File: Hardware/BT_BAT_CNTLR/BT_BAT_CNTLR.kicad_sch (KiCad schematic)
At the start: 0 parts

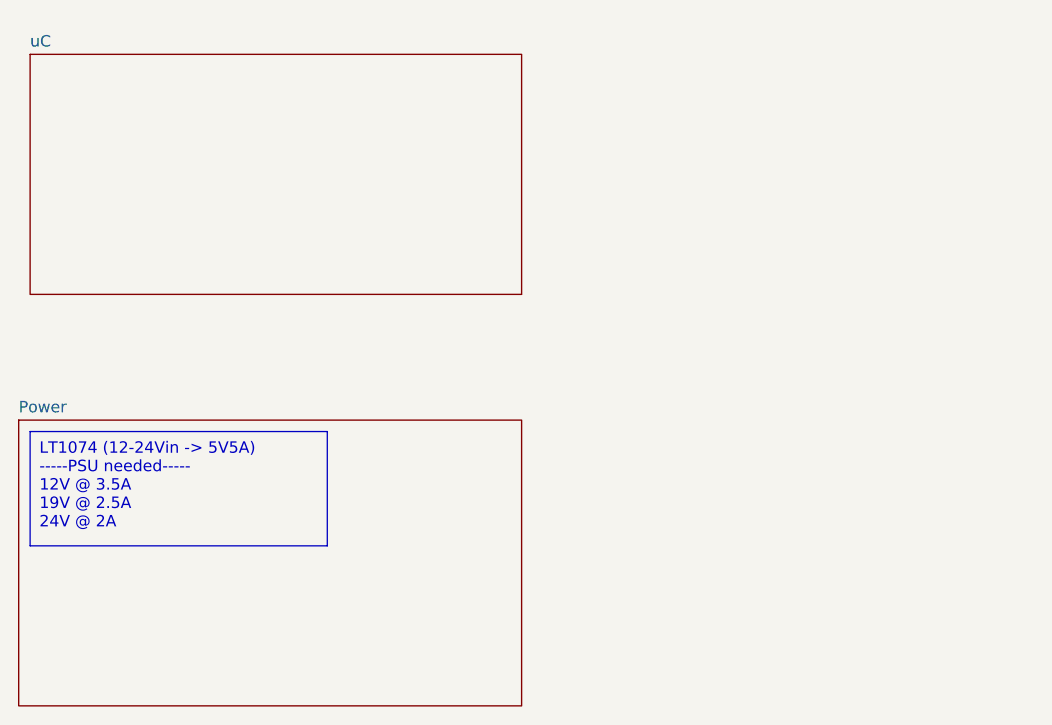
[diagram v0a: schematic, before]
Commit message: Added 1 USB circuit
will wait for approval/ review before continuing
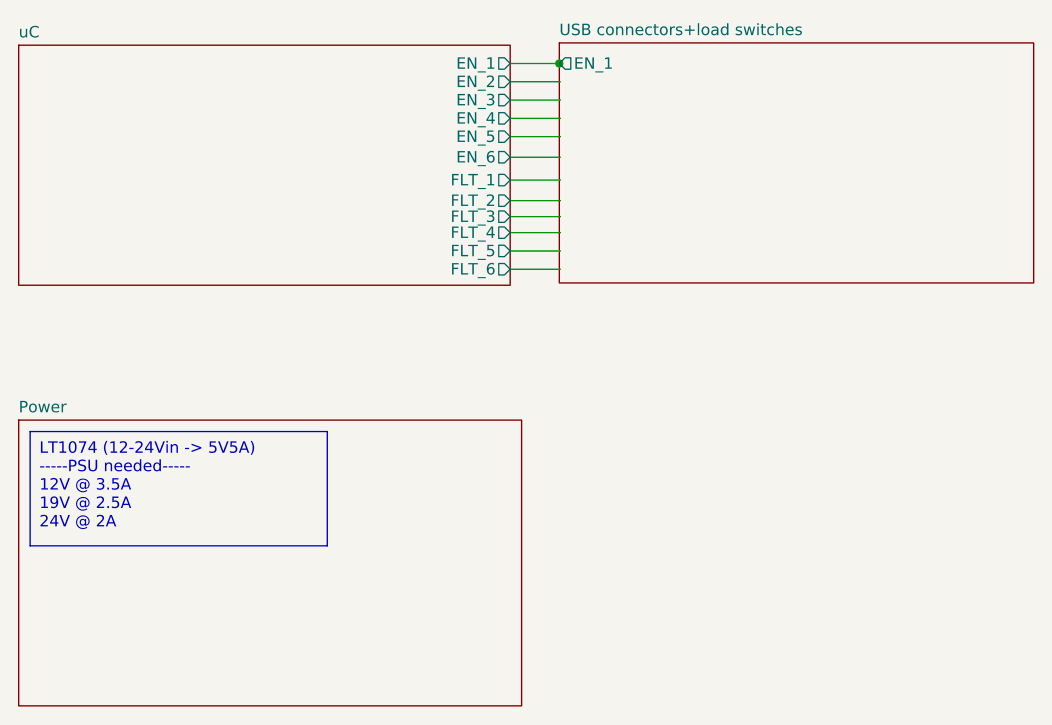
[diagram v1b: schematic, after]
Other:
- added sheet USB connectors+load switches (untitled.kicad_sch)
- sheet uC ports: added EN_1, EN_2, EN_3, EN_4, EN_5, EN_6, FLT_1, FLT_2, FLT_3, FLT_4, FLT_5, FLT_6; removed none
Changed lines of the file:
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@@
 (kicad_sch (version 20230121) (generator eeschema)
   (paper "A4")
+  (junction (at 151.511 27.686) (diameter 0) (color 0 0 0 0)
+  )
+  (wire (pts (xy 146.05 38.1) (xy 151.638 38.1))
+    (stroke (width 0) (type default))
+  )
+  (wire (pts (xy 146.05 29.718) (xy 151.638 29.718))
+    (stroke (width 0) (type default))
+  )
+  (wire (pts (xy 146.05 27.686) (xy 151.511 27.686))
+    (stroke (width 0) (type default))
+  )
+  (wire (pts (xy 146.05 33.782) (xy 151.638 33.782))
+    (stroke (width 0) (type default))
+  )
+  (wire (pts (xy 146.05 46.482) (xy 151.638 46.482))
+    (stroke (width 0) (type default))
+  )
+  (wire (pts (xy 146.05 42.926) (xy 151.638 42.926))
+    (stroke (width 0) (type default))
+  )
+  (wire (pts (xy 146.05 50.546) (xy 151.638 50.546))
+    (stroke (width 0) (type default))
+  )
+  (wire (pts (xy 146.05 48.514) (xy 151.638 48.514))
+    (stroke (width 0) (type default))
+  )
+  (wire (pts (xy 146.05 40.64) (xy 151.638 40.64))
+    (stroke (width 0) (type default))
+  )
+  (wire (pts (xy 146.05 35.814) (xy 151.638 35.814))
+    (stroke (width 0) (type default))
+  )
+  (wire (pts (xy 146.05 44.704) (xy 151.638 44.704))
+    (stroke (width 0) (type default))
+  )
+  (wire (pts (xy 151.511 27.686) (xy 151.638 27.686))
+    (stroke (width 0) (type default))
+  )
+  (wire (pts (xy 146.05 31.75) (xy 151.638 31.75))
+    (stroke (width 0) (type default))
+  )
   (text_box "LT1074 (12-24Vin -> 5V5A)\n-----PSU needed-----\n12V @ 3.5A\n19V @ 2.5A \n24V @ 2A\n"
     (at 92.71 68.58 0) (size 33.02 12.7)
@@
     (fill (type none))
     (effects (font (size 1.27 1.27)) (justify left top))
+  )
+  (sheet (at 151.511 25.4) (size 52.705 26.67) (fields_autoplaced)
+    (stroke (width 0.1524) (type solid))
+    (fill (color 0 0 0 0.0000))
+    (property "Sheetname" "USB connectors+load switches" (at 151.511 24.6884 0)
+      (effects (font (size 1.27 1.27)) (justify left bottom))
+    )
+    (property "Sheetfile" "untitled.kicad_sch" (at 151.511 52.6546 0)
+      (effects (font (size 1.27 1.27)) (justify left top) hide)
+    )
+    (pin "EN_1" output (at 151.511 27.686 180)
+      (effects (font (size 1.27 1.27)) (justify left))
+    )
+    (instances
+      (project "BT_BAT_CNTLR"
+        (path "/143e9064-c770-4695-a09b-614b7f1f856a" (page "4"))
+      )
+    )
   )
   (sheet (at 91.44 67.31) (size 55.88 31.75) (fields_autoplaced)
@@
     )
   )
-  (sheet (at 92.71 26.67) (size 54.61 26.67) (fields_autoplaced)
+  (sheet (at 91.44 25.654) (size 54.61 26.67) (fields_autoplaced)
     (stroke (width 0.1524) (type solid))
     (fill (color 0 0 0 0.0000))
-    (property "Sheetname" "uC" (at 92.71 25.9584 0)
+    (property "Sheetname" "uC" (at 91.44 24.9424 0)
       (effects (font (size 1.27 1.27)) (justify left bottom))
     )
-    (property "Sheetfile" "uC.kicad_sch" (at 92.71 53.9246 0)
+    (property "Sheetfile" "uC.kicad_sch" (at 91.44 52.9086 0)
       (effects (font (size 1.27 1.27)) (justify left top) hide)
     )
+    (pin "EN_1" output (at 146.05 27.686 0)
+      (effects (font (size 1.27 1.27)) (justify right))
+    )
+    (pin "EN_2" output (at 146.05 29.718 0)
+      (effects (font (size 1.27 1.27)) (justify right))
+    )
+    (pin "EN_3" output (at 146.05 31.75 0)
+      (effects (font (size 1.27 1.27)) (justify right))
+    )
+    (pin "EN_4" output (at 146.05 33.782 0)
+      (effects (font (size 1.27 1.27)) (justify right))
+    )
+    (pin "EN_5" output (at 146.05 35.814 0)
+      (effects (font (size 1.27 1.27)) (justify right))
+    )
+    (pin "EN_6" output (at 146.05 38.1 0)
+      (effects (font (size 1.27 1.27)) (justify right))
+    )
+    (pin "FLT_1" output (at 146.05 40.64 0)
+      (effects (font (size 1.27 1.27)) (justify right))
+    )
+    (pin "FLT_2" output (at 146.05 42.926 0)
+      (effects (font (size 1.27 1.27)) (justify right))
+    )
+    (pin "FLT_3" output (at 146.05 44.704 0)
+      (effects (font (size 1.27 1.27)) (justify right))
+    )
+    (pin "FLT_6" output (at 146.05 50.546 0)
+      (effects (font (size 1.27 1.27)) (justify right))
+    )
+    (pin "FLT_5" output (at 146.05 48.514 0)
+      (effects (font (size 1.27 1.27)) (justify right))
+    )
+    (pin "FLT_4" output (at 146.05 46.482 0)
+      (effects (font (size 1.27 1.27)) (justify right))
+    )
     (instances

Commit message: - Github Tree Cleanup - Power Routing
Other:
- sheet USB connectors+load switches ports: added EN_2, EN_3, EN_4, EN_5, EN_6, FLT_1, FLT_2, FLT_3, FLT_4, FLT_5, FLT_6; removed none
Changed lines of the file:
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@@
 (kicad_sch (version 20230121) (generator eeschema)
   (paper "A4")
-  (junction (at 151.511 27.686) (diameter 0) (color 0 0 0 0)
-  )
-  (wire (pts (xy 146.05 38.1) (xy 151.638 38.1))
+  (wire (pts (xy 146.05 35.56) (xy 151.13 35.56))
     (stroke (width 0) (type default))
   )
-  (wire (pts (xy 146.05 29.718) (xy 151.638 29.718))
+  (wire (pts (xy 146.05 30.48) (xy 151.13 30.48))
     (stroke (width 0) (type default))
   )
-  (wire (pts (xy 146.05 27.686) (xy 151.511 27.686))
+  (wire (pts (xy 146.05 45.72) (xy 151.13 45.72))
     (stroke (width 0) (type default))
   )
-  (wire (pts (xy 146.05 33.782) (xy 151.638 33.782))
+  (wire (pts (xy 146.05 50.8) (xy 151.13 50.8))
     (stroke (width 0) (type default))
   )
-  (wire (pts (xy 146.05 46.482) (xy 151.638 46.482))
+  (wire (pts (xy 146.05 33.02) (xy 151.13 33.02))
     (stroke (width 0) (type default))
   )
-  (wire (pts (xy 146.05 42.926) (xy 151.638 42.926))
+  (wire (pts (xy 146.05 27.94) (xy 151.13 27.94))
     (stroke (width 0) (type default))
   )
-  (wire (pts (xy 146.05 50.546) (xy 151.638 50.546))
+  (wire (pts (xy 146.05 55.88) (xy 151.13 55.88))
     (stroke (width 0) (type default))
   )
-  (wire (pts (xy 146.05 48.514) (xy 151.638 48.514))
+  (wire (pts (xy 146.05 38.1) (xy 151.13 38.1))
     (stroke (width 0) (type default))
   )
-  (wire (pts (xy 146.05 40.64) (xy 151.638 40.64))
+  (wire (pts (xy 146.05 43.18) (xy 151.13 43.18))
     (stroke (width 0) (type default))
   )
-  (wire (pts (xy 146.05 35.814) (xy 151.638 35.814))
+  (wire (pts (xy 146.05 53.34) (xy 151.13 53.34))
     (stroke (width 0) (type default))
   )
-  (wire (pts (xy 146.05 44.704) (xy 151.638 44.704))
+  (wire (pts (xy 146.05 40.64) (xy 151.13 40.64))
     (stroke (width 0) (type default))
   )
-  (wire (pts (xy 151.511 27.686) (xy 151.638 27.686))
-    (stroke (width 0) (type default))
-  )
-  (wire (pts (xy 146.05 31.75) (xy 151.638 31.75))
+  (wire (pts (xy 146.05 48.26) (xy 151.13 48.26))
     (stroke (width 0) (type default))
   )
@@
     (effects (font (size 1.27 1.27)) (justify left top))
   )
-  (sheet (at 151.511 25.4) (size 52.705 26.67) (fields_autoplaced)
+  (sheet (at 151.13 26.924) (size 52.705 30.226) (fields_autoplaced)
     (stroke (width 0.1524) (type solid))
     (fill (color 0 0 0 0.0000))
-    (property "Sheetname" "USB connectors+load switches" (at 151.511 24.6884 0)
+    (property "Sheetname" "USB connectors+load switches" (at 151.13 26.2124 0)
       (effects (font (size 1.27 1.27)) (justify left bottom))
     )
-    (property "Sheetfile" "untitled.kicad_sch" (at 151.511 52.6546 0)
+    (property "Sheetfile" "untitled.kicad_sch" (at 151.13 57.7346 0)
       (effects (font (size 1.27 1.27)) (justify left top) hide)
     )
-    (pin "EN_1" output (at 151.511 27.686 180)
+    (pin "EN_1" output (at 151.13 27.94 180)
+      (effects (font (size 1.27 1.27)) (justify left))
+    )
+    (pin "FLT_1" input (at 151.13 43.18 180)
+      (effects (font (size 1.27 1.27)) (justify left))
+    )
+    (pin "FLT_2" input (at 151.13 45.72 180)
+      (effects (font (size 1.27 1.27)) (justify left))
+    )
+    (pin "EN_2" input (at 151.13 30.48 180)
+      (effects (font (size 1.27 1.27)) (justify left))
+    )
+    (pin "EN_3" input (at 151.13 33.02 180)
+      (effects (font (size 1.27 1.27)) (justify left))
+    )
+    (pin "FLT_3" input (at 151.13 48.26 180)
+      (effects (font (size 1.27 1.27)) (justify left))
+    )
+    (pin "EN_6" input (at 151.13 40.64 180)
+      (effects (font (size 1.27 1.27)) (justify left))
+    )
+    (pin "EN_5" input (at 151.13 38.1 180)
+      (effects (font (size 1.27 1.27)) (justify left))
+    )
+    (pin "EN_4" input (at 151.13 35.56 180)
+      (effects (font (size 1.27 1.27)) (justify left))
+    )
+    (pin "FLT_6" input (at 151.13 55.88 180)
+      (effects (font (size 1.27 1.27)) (justify left))
+    )
+    (pin "FLT_5" input (at 151.13 53.34 180)
+      (effects (font (size 1.27 1.27)) (justify left))
+    )
+    (pin "FLT_4" input (at 151.13 50.8 180)
       (effects (font (size 1.27 1.27)) (justify left))
     )
@@
     )
   )
-  (sheet (at 91.44 25.654) (size 54.61 26.67) (fields_autoplaced)
+  (sheet (at 91.44 27.178) (size 54.61 29.972) (fields_autoplaced)
     (stroke (width 0.1524) (type solid))
     (fill (color 0 0 0 0.0000))
-    (property "Sheetname" "uC" (at 91.44 24.9424 0)
+    (property "Sheetname" "uC" (at 91.44 26.4664 0)
       (effects (font (size 1.27 1.27)) (justify left bottom))
     )
-    (property "Sheetfile" "uC.kicad_sch" (at 91.44 52.9086 0)
+    (property "Sheetfile" "uC.kicad_sch" (at 91.44 57.7346 0)
       (effects (font (size 1.27 1.27)) (justify left top) hide)
     )
-    (pin "EN_1" output (at 146.05 27.686 0)
+    (pin "EN_1" output (at 146.05 27.94 0)
       (effects (font (size 1.27 1.27)) (justify right))
     )
-    (pin "EN_2" output (at 146.05 29.718 0)
+    (pin "EN_2" output (at 146.05 30.48 0)
       (effects (font (size 1.27 1.27)) (justify right))
     )
-    (pin "EN_3" output (at 146.05 31.75 0)
+    (pin "EN_3" output (at 146.05 33.02 0)
       (effects (font (size 1.27 1.27)) (justify right))
     )
-    (pin "EN_4" output (at 146.05 33.782 0)
+    (pin "EN_4" output (at 146.05 35.56 0)
       (effects (font (size 1.27 1.27)) (justify right))
     )
-    (pin "EN_5" output (at 146.05 35.814 0)
+    (pin "EN_5" output (at 146.05 38.1 0)
       (effects (font (size 1.27 1.27)) (justify right))
     )
-    (pin "EN_6" output (at 146.05 38.1 0)
+    (pin "EN_6" output (at 146.05 40.64 0)
       (effects (font (size 1.27 1.27)) (justify right))
     )
-    (pin "FLT_1" output (at 146.05 40.64 0)
+    (pin "FLT_1" output (at 146.05 43.18 0)
       (effects (font (size 1.27 1.27)) (justify right))
     )
-    (pin "FLT_2" output (at 146.05 42.926 0)
+    (pin "FLT_2" output (at 146.05 45.72 0)
       (effects (font (size 1.27 1.27)) (justify right))
     )
-    (pin "FLT_3" output (at 146.05 44.704 0)
+    (pin "FLT_3" output (at 146.05 48.26 0)
       (effects (font (size 1.27 1.27)) (justify right))
     )
-    (pin "FLT_6" output (at 146.05 50.546 0)
+    (pin "FLT_6" output (at 146.05 55.88 0)
       (effects (font (size 1.27 1.27)) (justify right))
     )
-    (pin "FLT_5" output (at 146.05 48.514 0)
+    (pin "FLT_5" output (at 146.05 53.34 0)
       (effects (font (size 1.27 1.27)) (justify right))
     )
-    (pin "FLT_4" output (at 146.05 46.482 0)
+    (pin "FLT_4" output (at 146.05 50.8 0)
       (effects (font (size 1.27 1.27)) (justify right))
     )
